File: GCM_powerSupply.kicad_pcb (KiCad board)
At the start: 2 copper layers, 85 x 95 mm, 34 parts, among them J1 Screw_Terminal_01x02, J2 Barrel_Jack_Switch, J3 Molex_1053101108, J4 Screw_Terminal_01x04, SW1 SW_SPDT, U1 TPS563201, U2 TPS563201

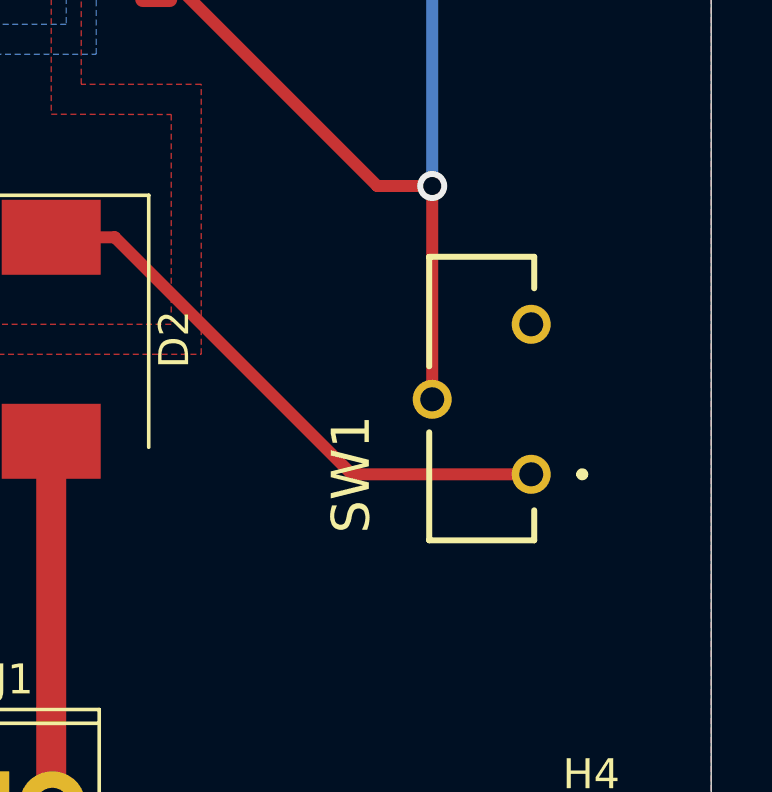
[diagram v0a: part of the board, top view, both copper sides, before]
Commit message: Fix R0805 was 1206, change the switch
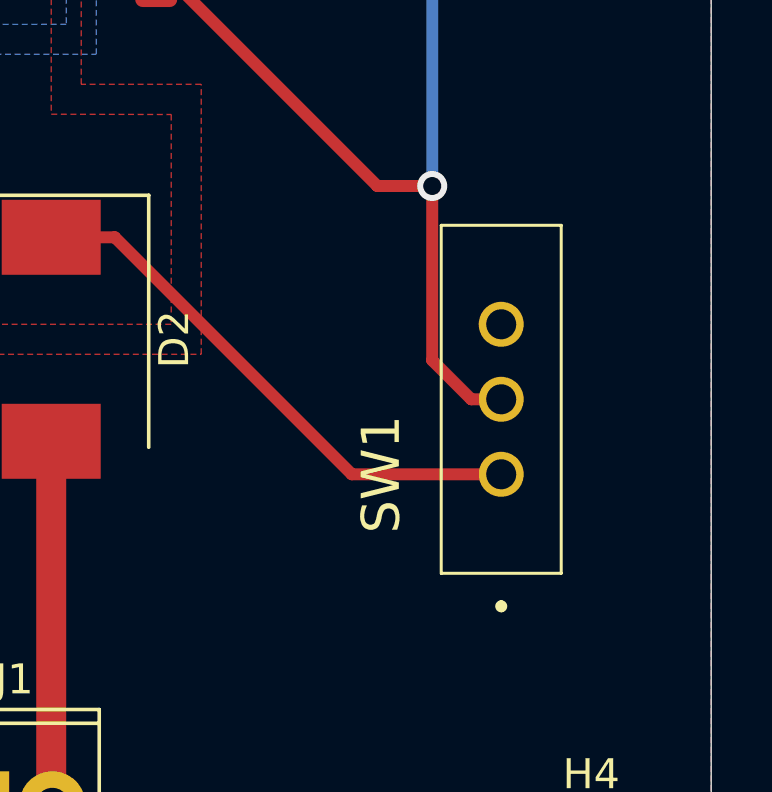
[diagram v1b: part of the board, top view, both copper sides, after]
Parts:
- SW1: footprint LSSA12VB:LSSA12VB -> EG1218:EG1218
- moved SW1 1.00 mm to (149.0, 120.0)
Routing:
- net /EN: track 62.3 -> 63.8 mm
- net VCC: track 39.8 -> 38.8 mm
